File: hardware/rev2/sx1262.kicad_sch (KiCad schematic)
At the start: 40 parts, among them Q1 SS8050, U3 SX1262IMLTRT, U4 PE4259, Y2 TXO-20CSMV-320

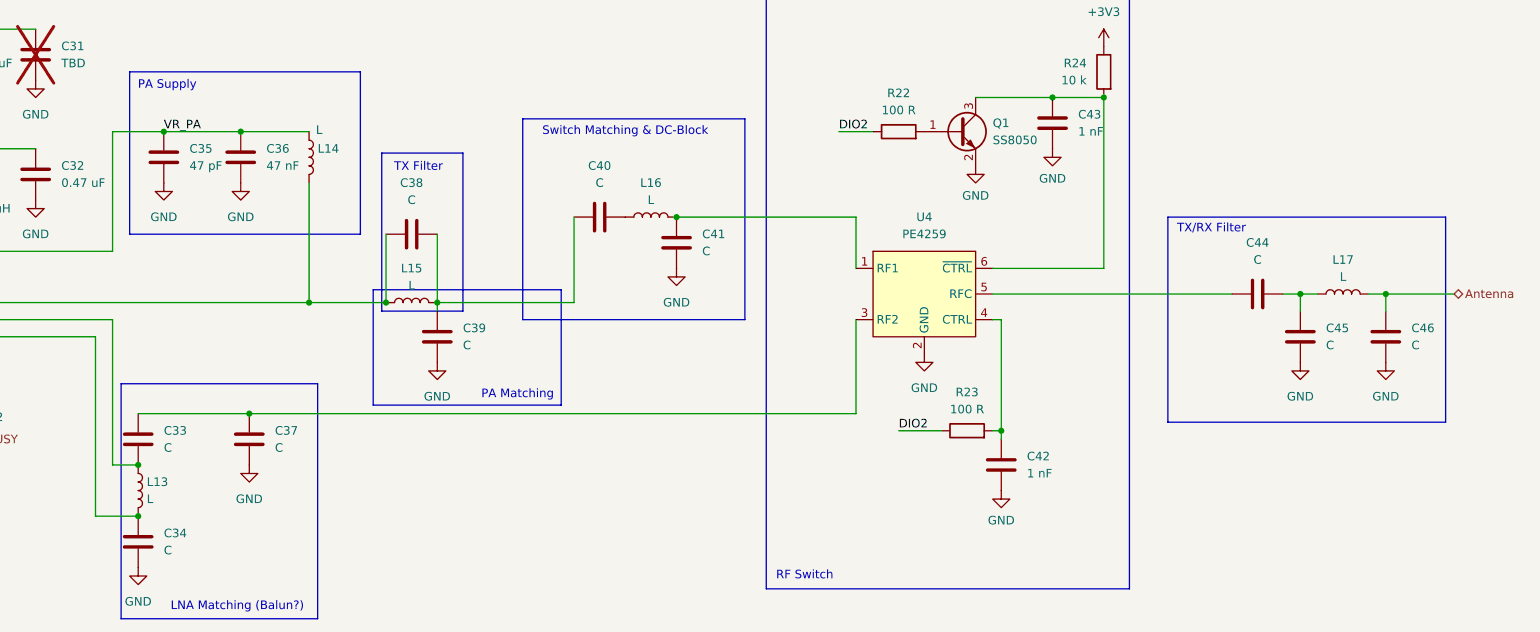
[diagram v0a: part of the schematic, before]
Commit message: finished PCB v1, changed rf connector layout, added vias, added footprints for RF filtering
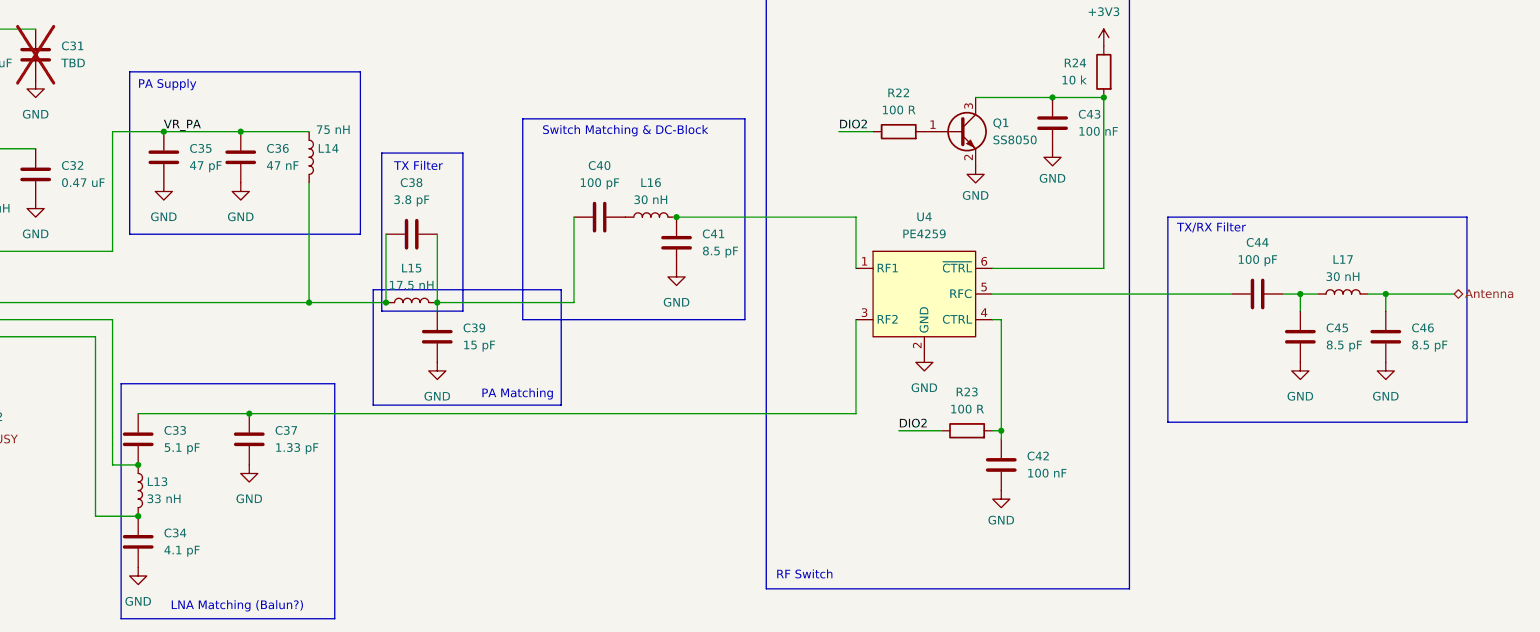
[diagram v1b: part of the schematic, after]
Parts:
- C33: value C -> 5.1 pF
- C34: value C -> 4.1 pF
- C37: value C -> 1.33 pF
- C38: value C -> 3.8 pF
- C39: value C -> 15 pF
- C40, C44: value C -> 100 pF
- C41, C45, C46: value C -> 8.5 pF
- C42, C43: value 1 nF -> 100 nF
- L13: value L -> 33 nH
- L14: value L -> 75 nH
- L15: value L -> 17.5 nH
- L16, L17: value L -> 30 nH
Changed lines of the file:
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@@
 	(rectangle
 		(start 163.83 149.225)
-		(end 193.04 184.15)
+		(end 195.58 184.15)
 		(stroke
 			(width 0)
@@
 	(rectangle
 		(start 319.405 124.46)
-		(end 360.68 154.94)
+		(end 363.855 154.94)
 		(stroke
 			(width 0)
@@
 			)
 		)
-		(property "Value" "C"
+		(property "Value" "8.5 pF"
 			(at 355.6 143.5099 0)
 			(show_name no)
@@
 			)
 		)
-		(property "Value" "C"
+		(property "Value" "4.1 pF"
 			(at 170.18 173.9899 0)
 			(show_name no)
@@
 			)
 		)
-		(property "Value" "L"
+		(property "Value" "33 nH"
 			(at 167.64 166.3699 0)
 			(show_name no)
@@
 			)
 		)
-		(property "Value" "L"
+		(property "Value" "30 nH"
 			(at 242.57 121.92 90)
 			(show_name no)
@@
 			)
 		)
-		(property "Value" "C"
+		(property "Value" "8.5 pF"
 			(at 250.19 129.5399 0)
 			(show_name no)
@@
 			)
 		)
-		(property "Value" "C"
+		(property "Value" "1.33 pF"
 			(at 186.69 158.7499 0)
 			(show_name no)
@@
 			)
 		)
-		(property "Value" "C"
+		(property "Value" "8.5 pF"
 			(at 342.9 143.5099 0)
 			(show_name no)
@@
 			)
 		)
-		(property "Value" "L"
+		(property "Value" "30 nH"
 			(at 345.44 133.35 90)
 			(show_name no)
@@
 			)
 		)
-		(property "Value" "L"
+		(property "Value" "75 nH"
 			(at 192.786 111.506 0)
 			(show_name no)
@@
 			)
 		)
-		(property "Value" "L"
+		(property "Value" "17.5 nH"
 			(at 207.01 134.62 90)
 			(show_name no)
@@
 			)
 		)
-		(property "Value" "1 nF"
+		(property "Value" "100 nF"
 			(at 298.45 162.5599 0)
 			(show_name no)
@@
 			)
 		)
-		(property "Value" "C"
+		(property "Value" "100 pF"
 			(at 332.74 130.81 90)
 			(show_name no)
@@
 			)
 		)
-		(property "Value" "1 nF"
+		(property "Value" "100 nF"
 			(at 306.07 111.7599 0)
 			(show_name no)
@@
 			)
 		)
-		(property "Value" "C"
+		(property "Value" "100 pF"
 			(at 234.95 119.38 90)
 			(show_name no)
@@
 			)
 		)
-		(property "Value" "C"
+		(property "Value" "3.8 pF"
 			(at 207.01 121.92 90)
 			(show_name no)
@@
 			)
 		)
-		(property "Value" "C"
+		(property "Value" "15 pF"
 			(at 214.63 143.5099 0)
 			(show_name no)
@@
 			)
 		)
-		(property "Value" "C"
+		(property "Value" "5.1 pF"
 			(at 170.18 158.7499 0)
 			(show_name no)

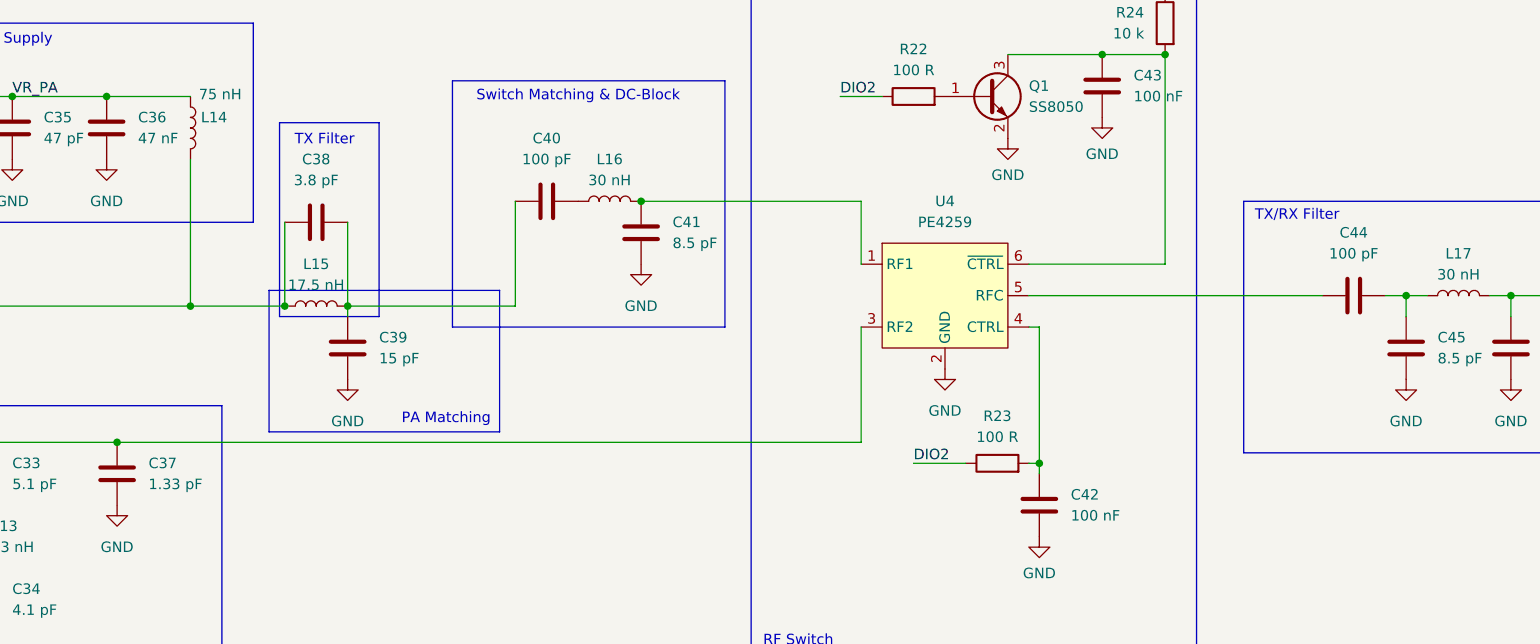
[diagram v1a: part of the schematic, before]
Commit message: fixed soldermask and silkscreen mostly
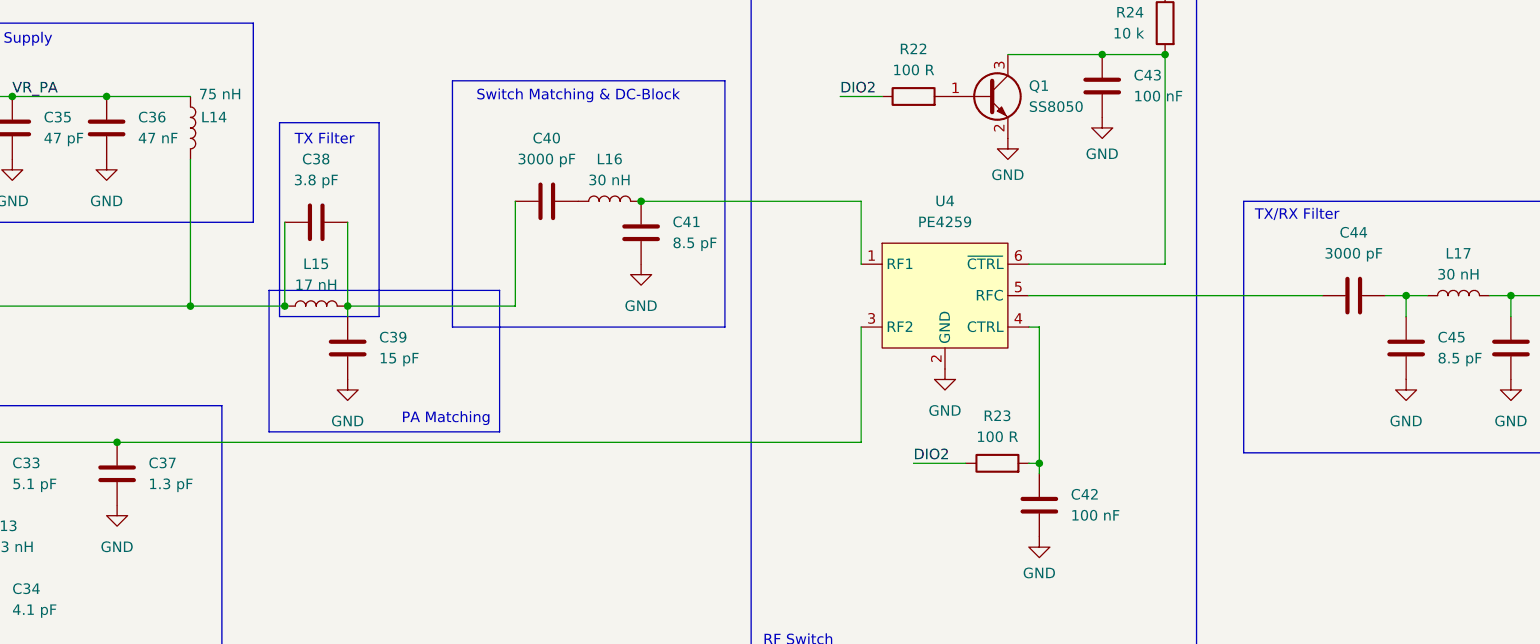
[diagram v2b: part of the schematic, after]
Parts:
- C33: Mouser Part Number (none) -> 81-GCM1555C1H5R1FA6D
- C34: Mouser Part Number (none) -> 81-GJM1555C1H4R1BB1D
- C37: value 1.33 pF -> 1.3 pF; Mouser Part Number (none) -> 81-GJM1555C1H1R3CB1D
- C38: Mouser Part Number (none) -> 81-GJM1555C1H3R8BB1D
- C39: Mouser Part Number (none) -> 81-GRT1555C1H150FA2D
- C40, C44: value 100 pF -> 3000 pF; Mouser Part Number (none) -> 81-GRM1557U1A302JA1D
- C41, C45, C46: Mouser Part Number (none) -> 81-GJM1555C1H8R5WB1D
- L13: Mouser Part Number (none) -> 81-LQW15AN33NJ00D
- L14: Mouser Part Number (none) -> 81-LQW15AN75NG00D
- L15: value 17.5 nH -> 17 nH; Mouser Part Number (none) -> 81-LQW15AN17NG8ZD
- L16, L17: Mouser Part Number (none) -> 81-LQW15AN30NG00D
- Q1: Mouser Part Number (none) -> 750-SS8050-G

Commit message: final edit, send to production
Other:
- company: MMCX11 -> Group 10
- title: (none) -> LoRa Based Cat Tracker

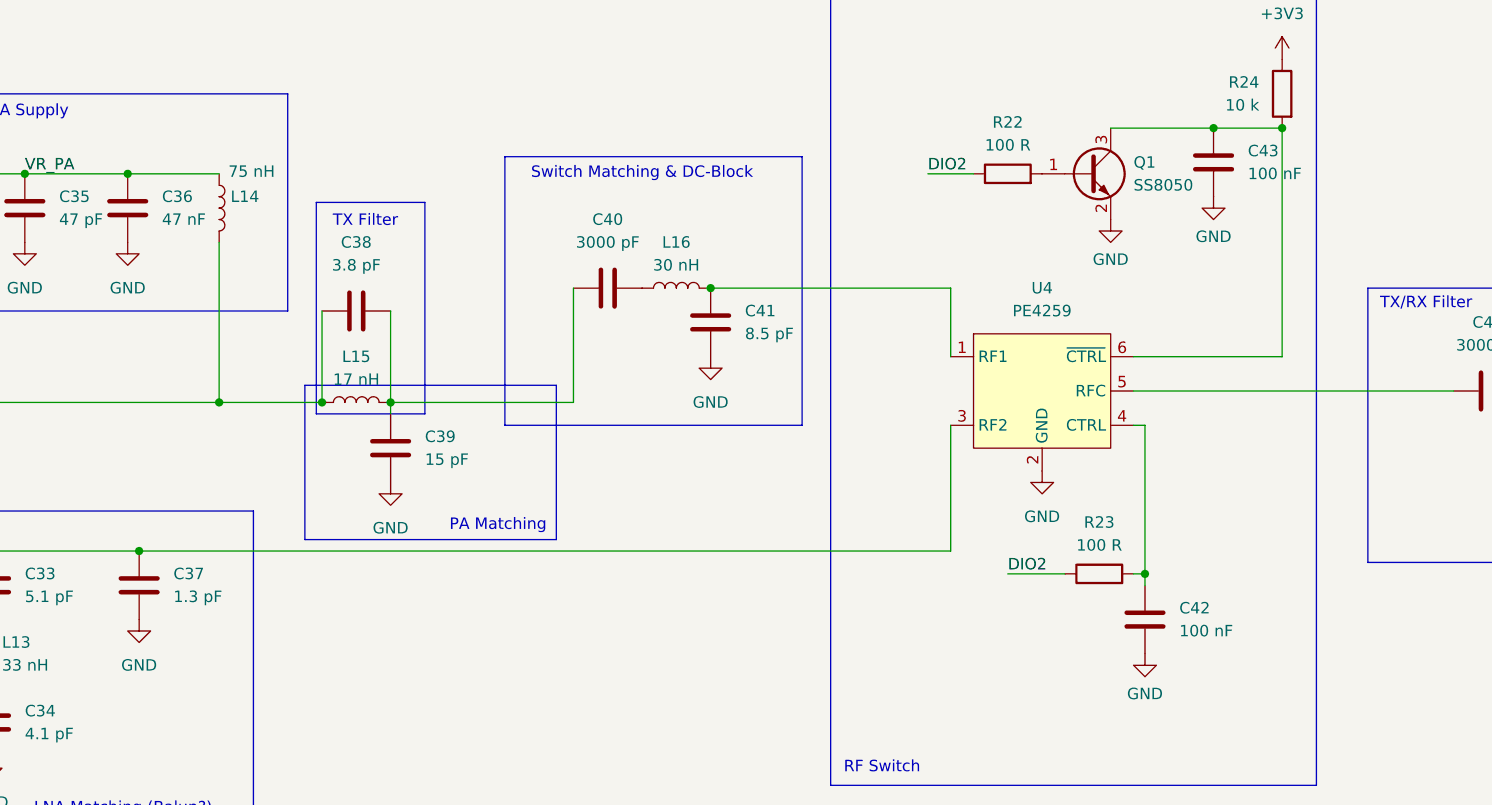
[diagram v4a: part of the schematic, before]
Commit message: changed values to be accurate to order
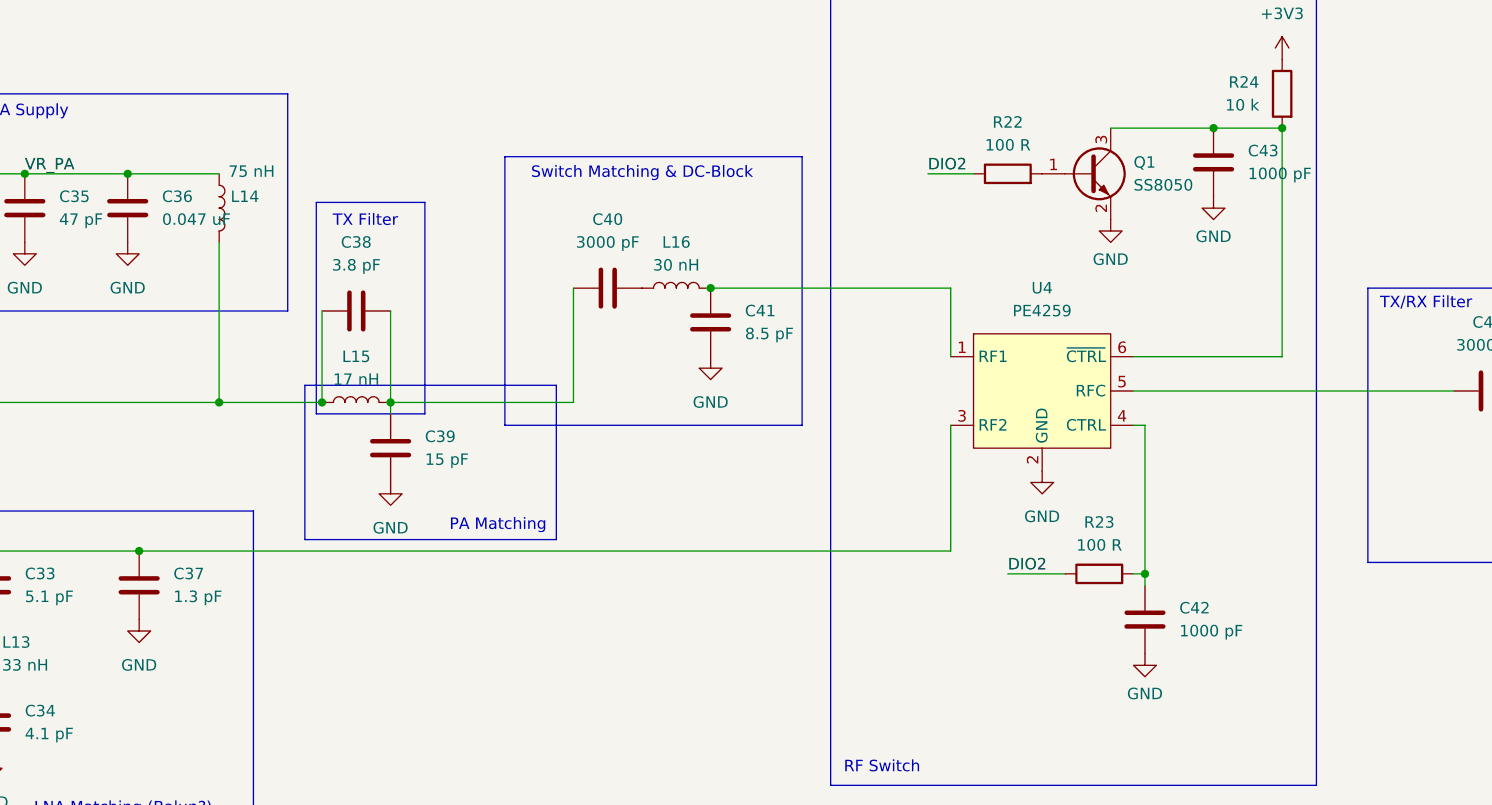
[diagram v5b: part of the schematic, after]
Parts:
- C36: value 47 nF -> 0.047 uF
- C42, C43: value 100 nF -> 1000 pF
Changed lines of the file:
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@@
 			)
 		)
-		(property "Value" "47 nF"
+		(property "Value" "0.047 uF"
 			(at 185.42 116.8399 0)
 			(show_name no)
@@
 			)
 		)
-		(property "Value" "100 nF"
+		(property "Value" "1000 pF"
 			(at 298.45 162.5599 0)
 			(show_name no)
@@
 			)
 		)
-		(property "Value" "100 nF"
+		(property "Value" "1000 pF"
 			(at 306.07 111.7599 0)
 			(show_name no)

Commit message: made schematics more prettier among other things
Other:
- moved on the sheet: C26, C27, C28, C29, C30, C31, C32, C33, C34, C35, C36, C37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

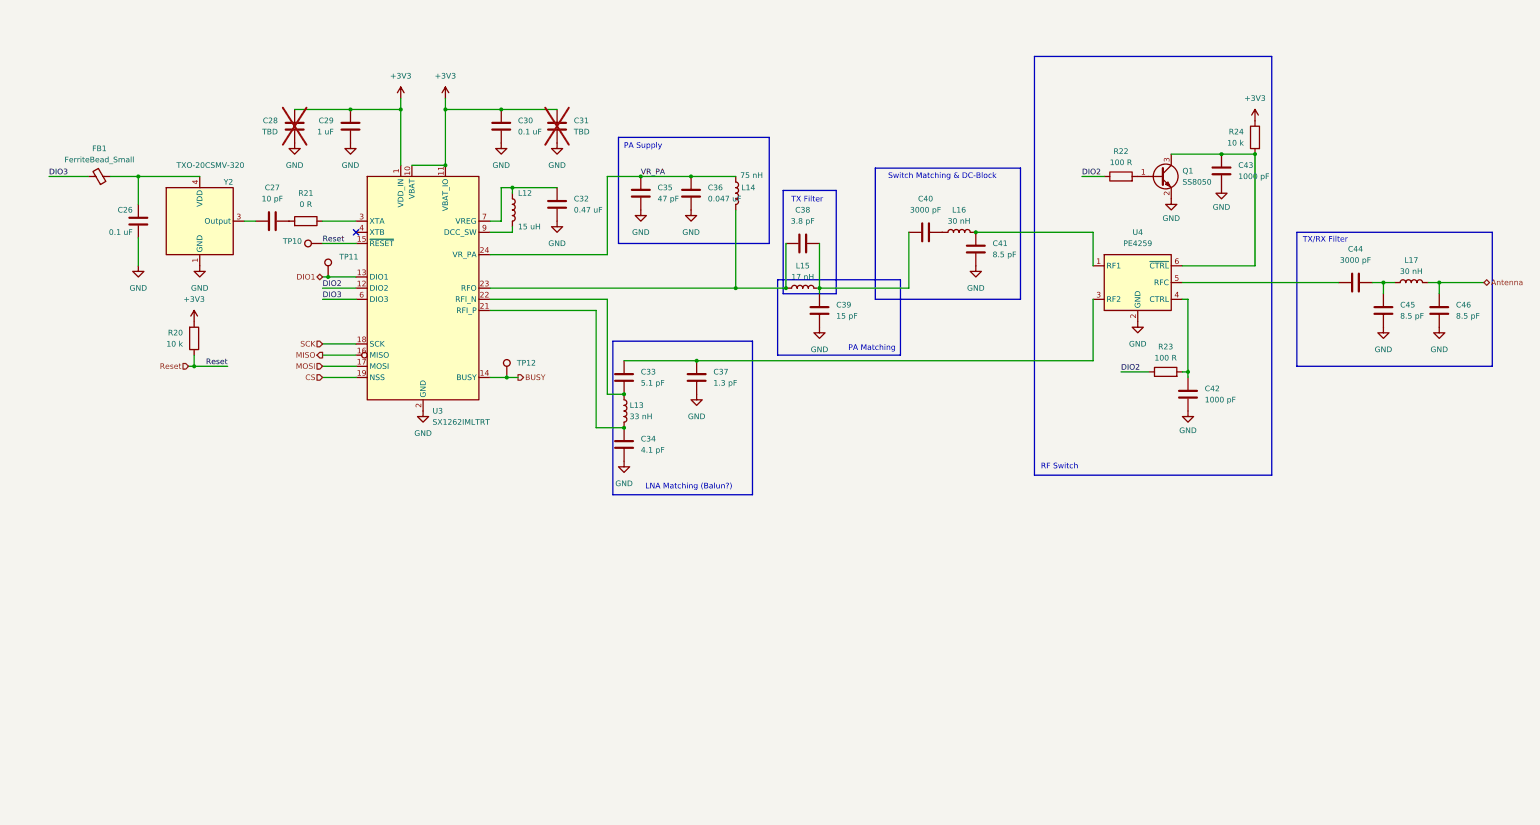
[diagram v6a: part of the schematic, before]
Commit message: updated schematics to reflect reality and made prettier
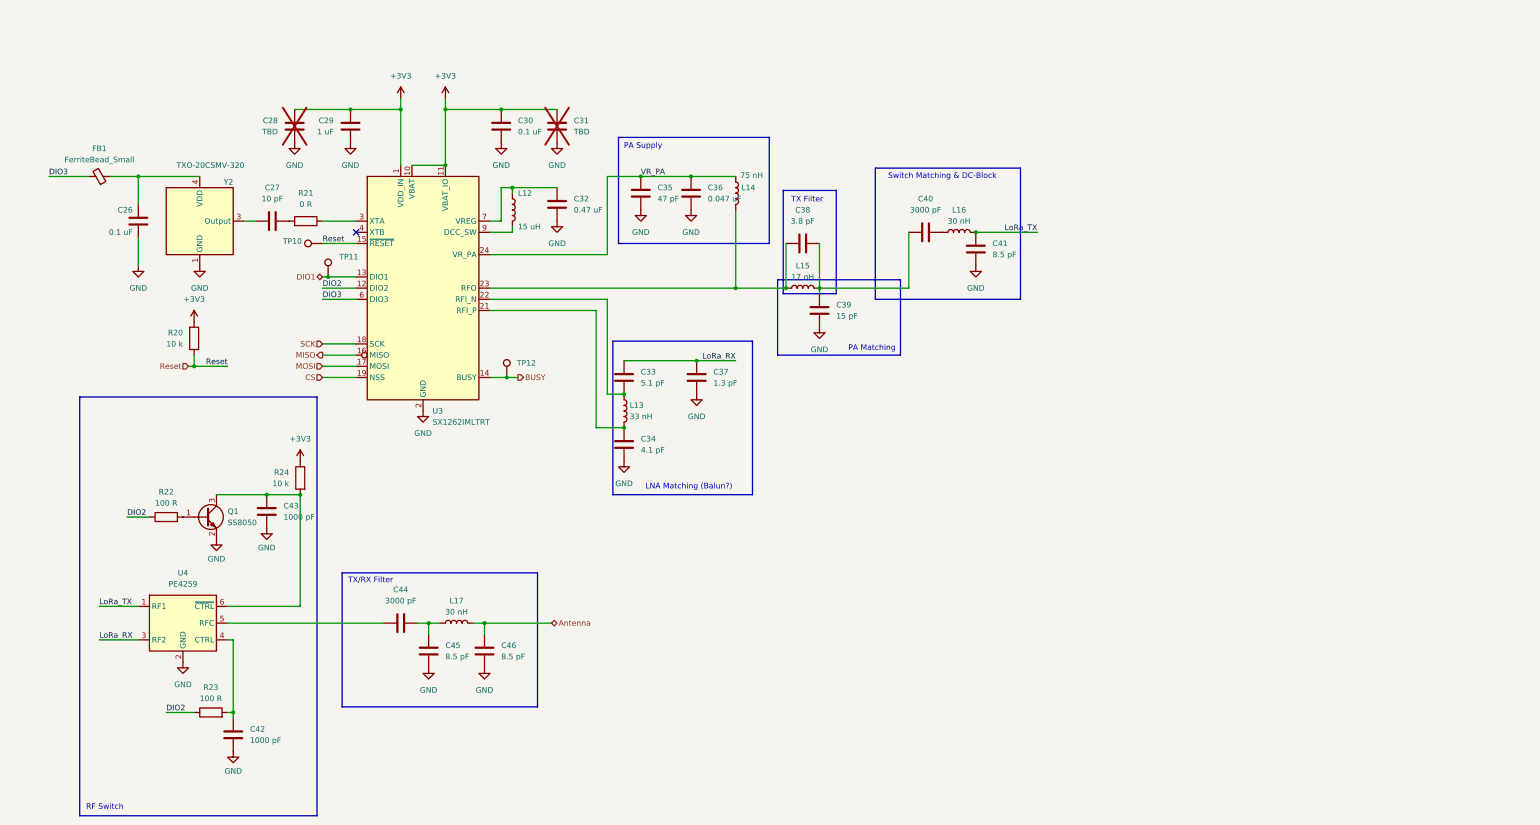
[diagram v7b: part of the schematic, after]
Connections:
- net LoRa_TX: now reaches C41.2, L16.2, U4.1 (RF1)
- net LoRa_RX: now reaches C33.1, C37.1, U4.3 (RF2)
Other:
- moved on the sheet: C42, C43, C44, C45, C46, L17, Q1, R22, R23, R24, U4
